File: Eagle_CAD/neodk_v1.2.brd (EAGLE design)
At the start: 80 x 41 mm, 73 parts, among them J1 SWD, J2 Power 5V..12V DC, J3 FC68131, J4 S2B-XH-A(LF)(SN), J5 S2B-XH-A(LF)(SN), Q1 IRLML6344TRPBF, Q2 IRLML6344TRPBF, Q3 PMV50EPEAR, SW2 FSMRA6JH, U1 SGM61410XN6G/TR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

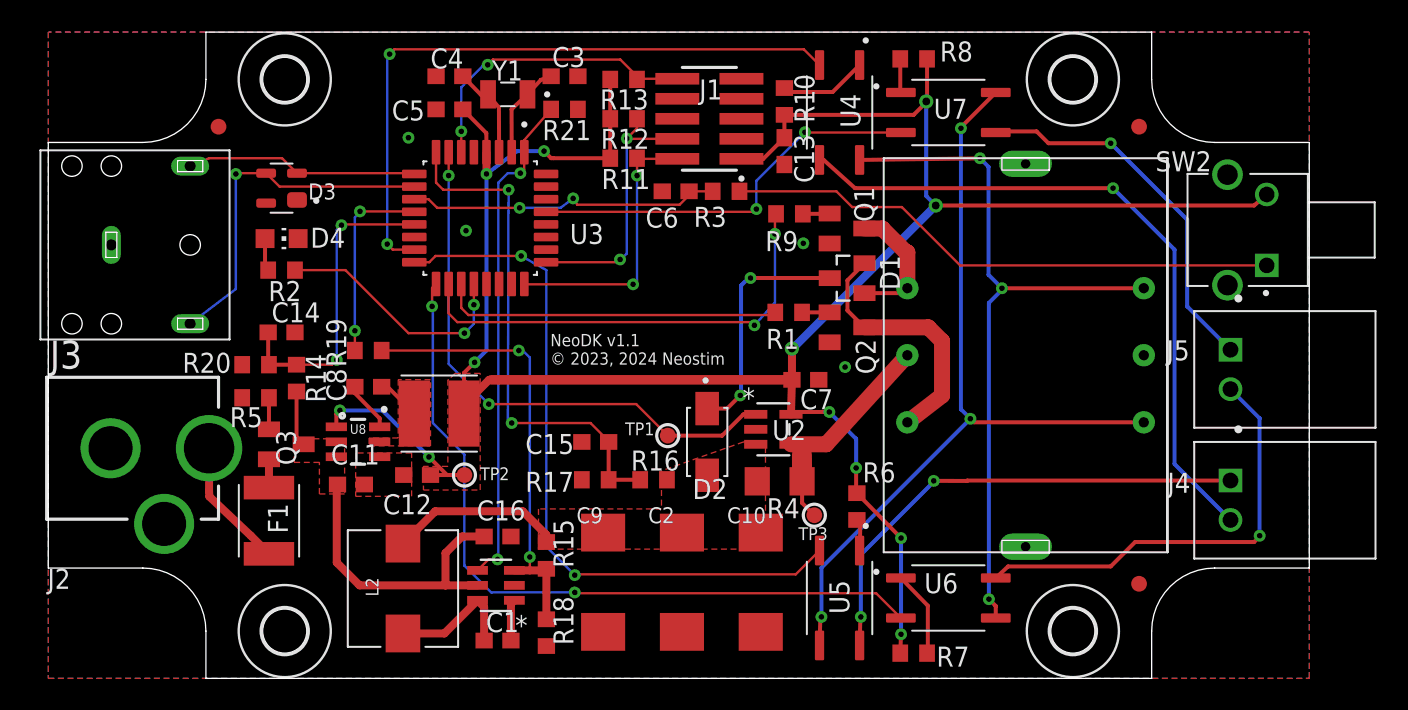
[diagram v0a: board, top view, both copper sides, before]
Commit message: Added feature to switch to bootloader.
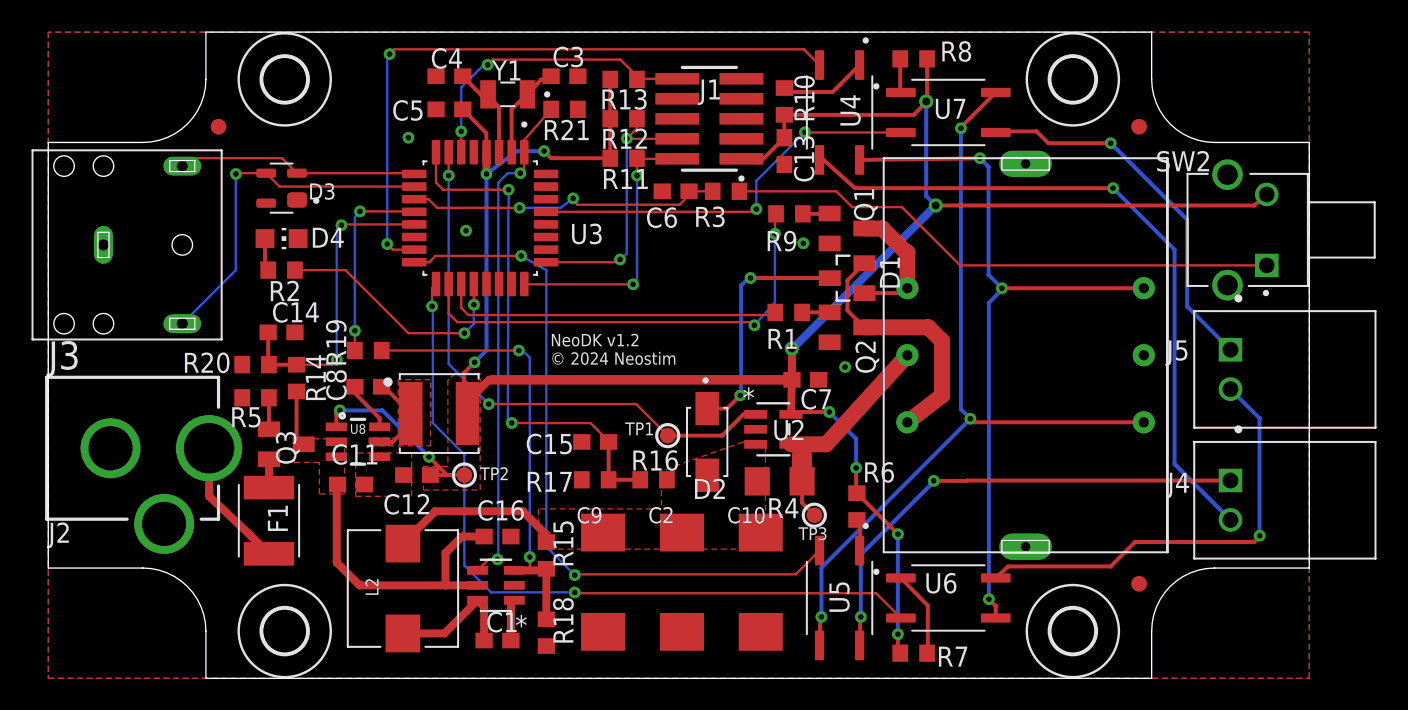
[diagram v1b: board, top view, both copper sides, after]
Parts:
- L1: value 3.9 µH -> 4.7 µH; device SRR4818A-3R9Y:IND_SRR4818A-3R9Y -> VLS5045EX-4R7M:IND_VLS5045EX-4R7M
- moved J3 0.50 mm to (3.50, 27.5)
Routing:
- net N$25: track 2.78 -> 5.15 mm
- net N$29: track 14.7 -> 15.3 mm
- net VCC: track 150.3 -> 149.8 mm
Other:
- board text added: "NeoDK v1.2 © 2024 Neostim"
- board text removed: "NeoDK v1.1 © 2023, 2024 Neostim"
